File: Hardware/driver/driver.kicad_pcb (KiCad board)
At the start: 4 copper layers, 128.1 x 184.5 mm, 158 parts, among them J201 Conn_02x10_Odd_Even, J301 1017526, J401 TBP02R2W-381-03BE, J402 Conn_01x02_Male, J501 Conn_Coaxial, J601 Screw_Terminal_01x02, K601 EC2-5TNU, M201 Fan_4pin, Q201 MMBT3904, Q202 PN2222A, Q301 IXTH80N075L2, Q302 IXTH80N075L2, U101 ICL7660, U102 DS2482-100, U201 AT24CS32-SSHM, U202 NCP716BCSN330T1G, U203 ADUM1250, U204 FODM217B, U205 FODM217B, U206 EMC2101-R, U301 MCP3421A2T-ECH, U302 OPA2388, U303 DAC60501Z, U304 LM431SC, U305 MCP3421A3T-ECH, U306 OPA2388, U307 DAC60501Z, U308 LM431SC, U309 DS18B20, U310 DS18B20, U501 74LVC1G17, U502 FODM217B, U601 MCP3421A1T-ECH, U602 OPA277

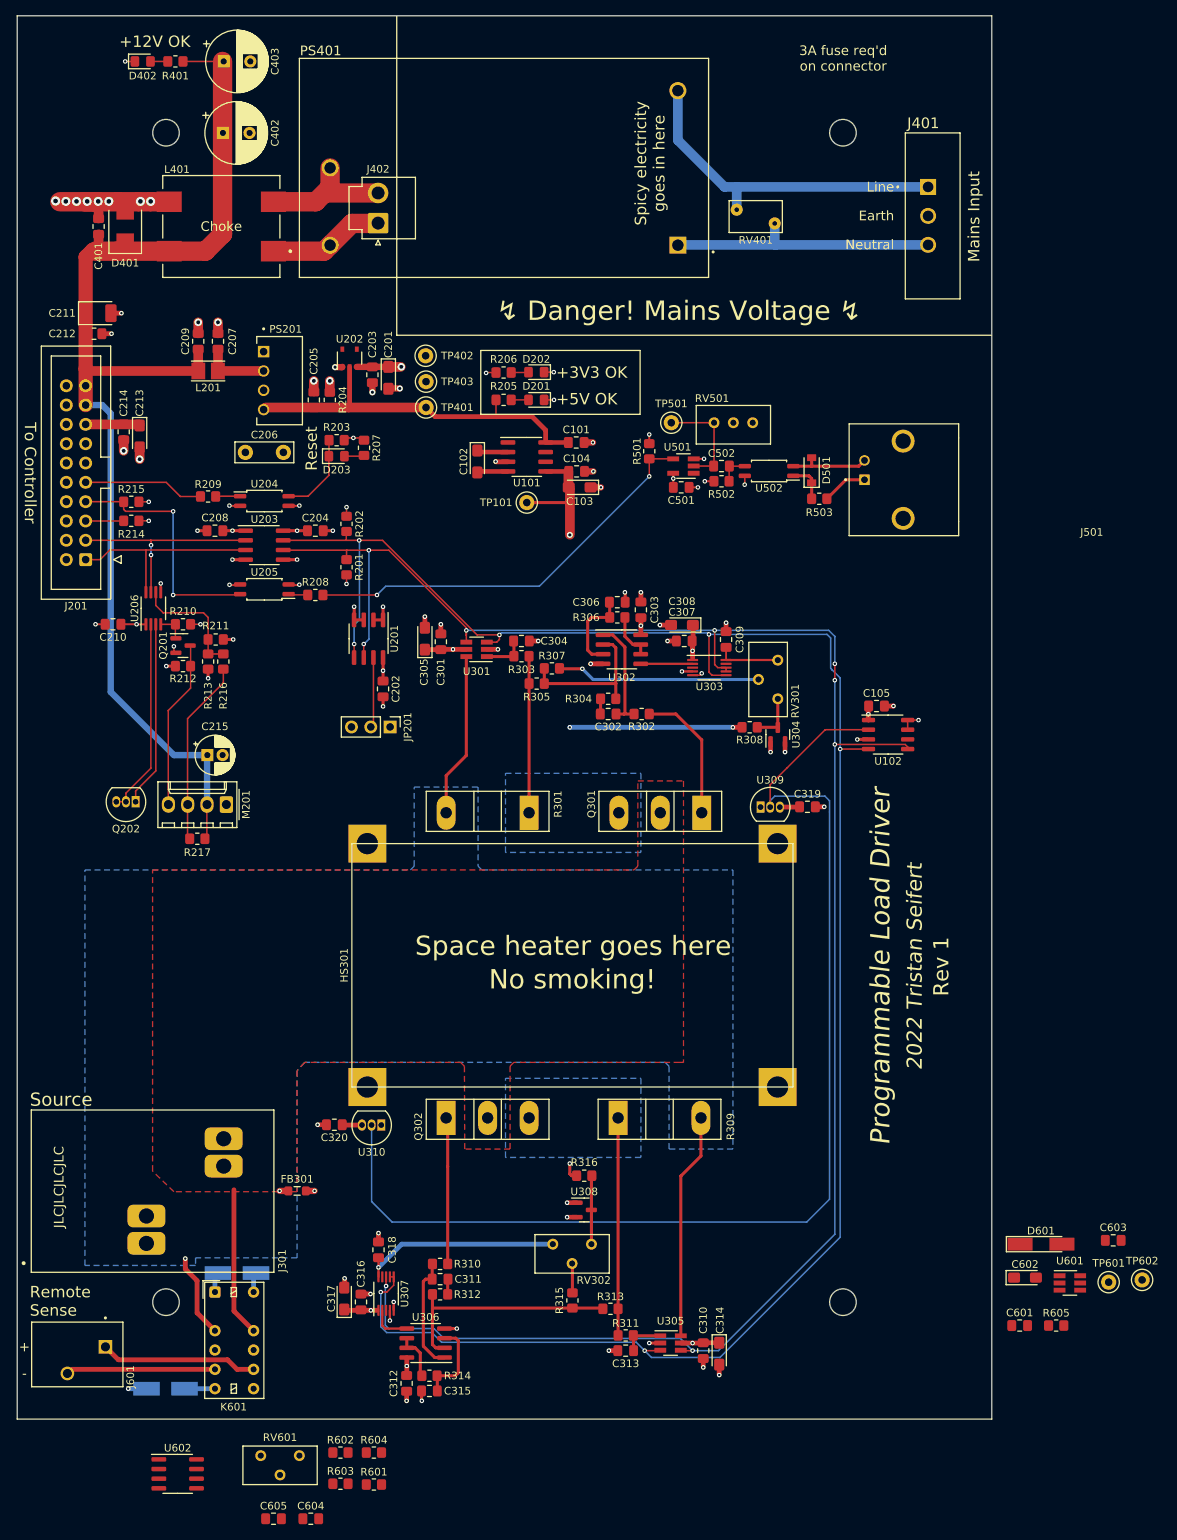
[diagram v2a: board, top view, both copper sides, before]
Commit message: Finished remote VSense support
- Laid out the VSense amp and analog-to-digital converter, as well as
  added an I2C IO expander to handle driving the latching relay to
  switch between internal and external sense.

  Also moved the input connector and some of the analog parts around to
  accomodate this all.

- Status indicator (with an extra GPIO on the IO expander) in the form
  of a single LED
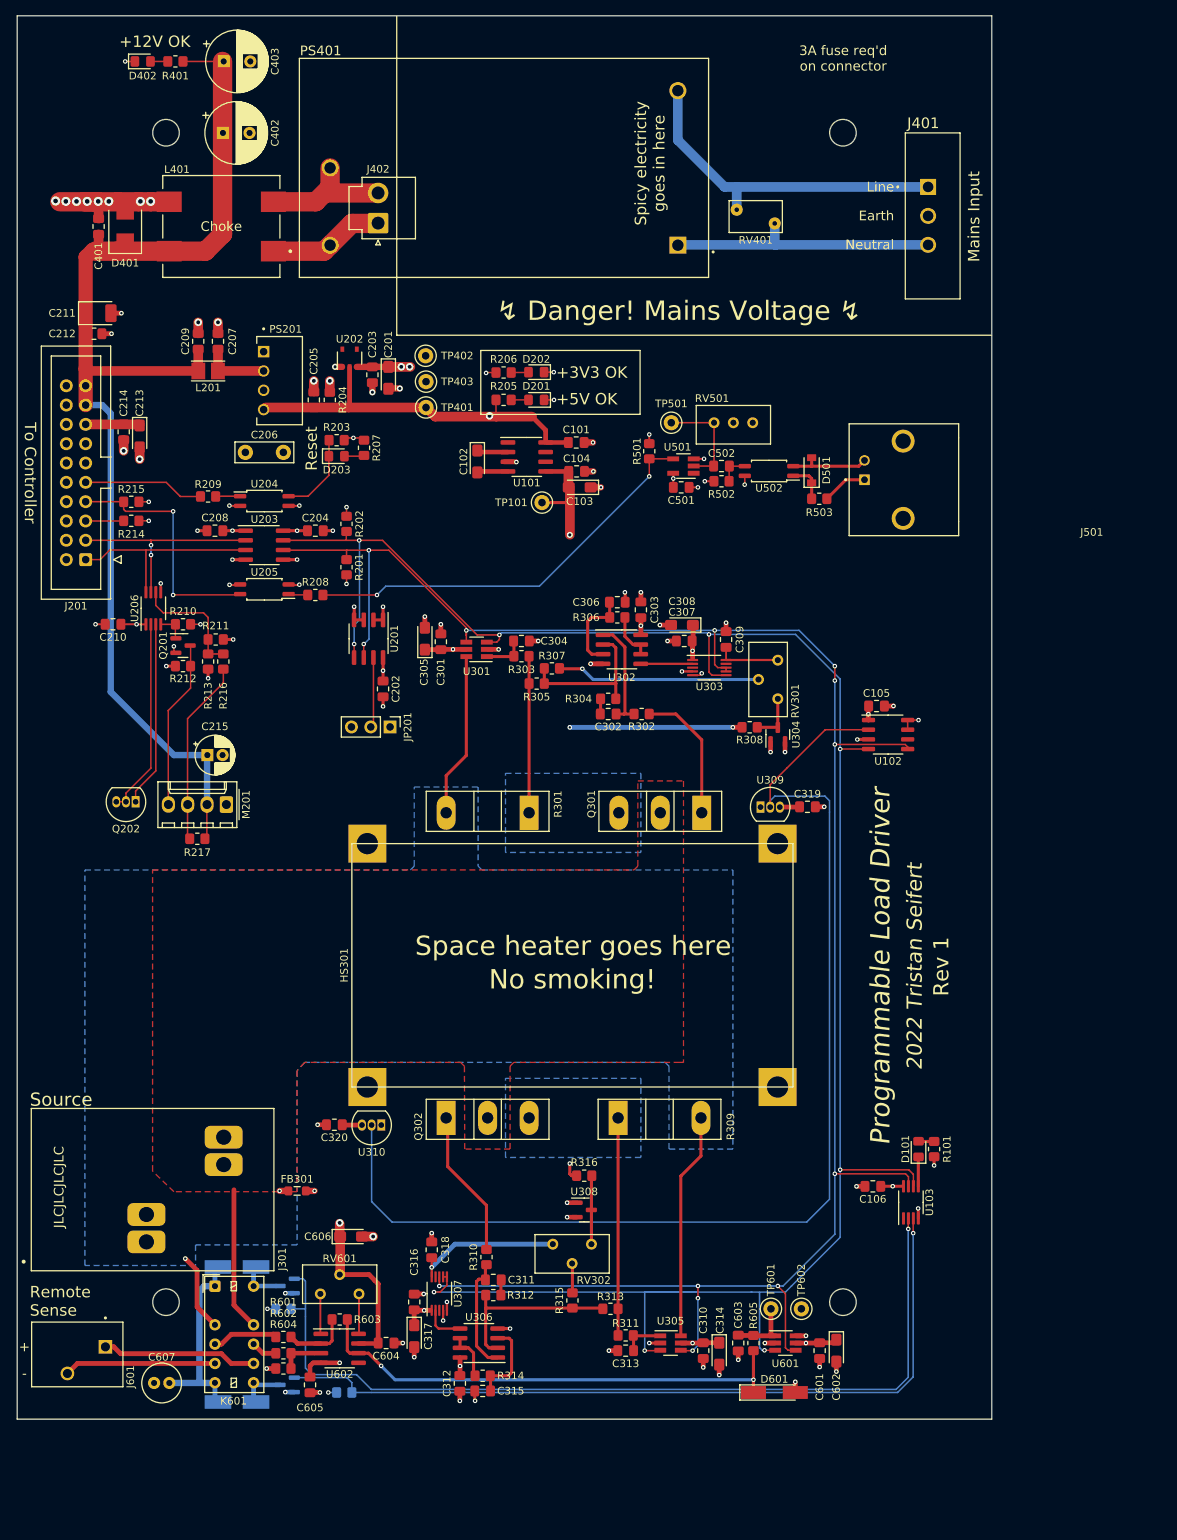
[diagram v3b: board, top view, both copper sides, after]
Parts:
- added C106: 100nF, Capacitor_SMD:C_0805_2012Metric_Pad1.18x1.45mm_HandSolder, F.Cu at (132.5, 173.9)
- added C606: 10µF, Capacitor_Tantalum_SMD:CP_EIA-3216-18_Kemet-A_Pad1.58x1.35mm_HandSolder, F.Cu at (63.9, 180.5)
- added C607: 10µF, Capacitor_THT:C_Radial_D5.0mm_H11.0mm_P2.00mm, F.Cu at (40.0, 199.8)
- added D101: Red, LED_SMD:LED_0805_2012Metric_Pad1.15x1.40mm_HandSolder, F.Cu at (138.5, 169.0)
- added Q601: MMBT3904, Package_TO_SOT_SMD:SOT-23, B.Cu at (55.5, 200.0)
- added Q602: MMBT3904, Package_TO_SOT_SMD:SOT-23, B.Cu at (55.5, 187.0)
- added R101: 1k, Resistor_SMD:R_0805_2012Metric_Pad1.20x1.40mm_HandSolder, F.Cu at (140.6, 169.0)
- added R606: 10k, Resistor_SMD:R_0805_2012Metric_Pad1.20x1.40mm_HandSolder, B.Cu at (55.0, 190.0)
- added R607: 10k, Resistor_SMD:R_0805_2012Metric_Pad1.20x1.40mm_HandSolder, B.Cu at (63.0, 201.0)
- added U103: PI4IOE5V9536, Package_SO:MSOP-8_3x3mm_P0.65mm, F.Cu at (137.5, 176.0)
- moved C603 51.1 mm to (114.8, 194.5), turned to -90 degrees
- moved TP602 45.0 mm to (123.1, 190.0)
- moved TP601 44.5 mm to (119.1, 190.0)
- moved D601 40.1 mm to (119.5, 201.0)
- moved R605 39.9 mm to (116.8, 194.5), turned to -90 degrees
- moved U601 38.2 mm to (121.0, 194.5)
- moved U602 26.9 mm to (62.4, 195.2)
- moved C602 26.6 mm to (127.7, 195.5), turned to -90 degrees
- moved C601 26.5 mm to (125.5, 195.5), turned to -90 degrees
- moved C604 25.1 mm to (68.5, 194.5)
- moved R601 22.8 mm to (55.0, 193.7), turned to 180 degrees
- moved R603 21.6 mm to (62.4, 191.4), turned to 180 degrees
- moved RV601 21.4 mm to (59.9, 188.0), turned to 180 degrees
- moved C605 18.2 mm to (58.5, 200.0), turned to -90 degrees
- moved R604 16.2 mm to (55.0, 197.8), turned to 180 degrees
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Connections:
- D602 pad 1: /Input Stage/Voltage Sense/SEL_SET -> +5V
- D602 pad 2: GND -> /Input Stage/Voltage Sense/SEL_SET
- D603 pad 1: /Input Stage/Voltage Sense/SEL_RESET -> +5V
- D603 pad 2: GND -> /Input Stage/Voltage Sense/SEL_RESET
- K601 pad 1: /Input Stage/Voltage Sense/SEL_SET -> +5V
- K601 pad 12: GND -> /Input Stage/Voltage Sense/SEL_SET
- K601 pad 6: /Input Stage/Voltage Sense/SEL_RESET -> +5V
- K601 pad 7: GND -> /Input Stage/Voltage Sense/SEL_RESET
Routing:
- net +5V: track 50.3 -> 233.5 mm, vias 0 -> 2
- net /SENSE_SET: track 0.00 -> 116.9 mm, vias 0 -> 1
- net /SENSE_RST: track 0.00 -> 104.6 mm, vias 0 -> 1
- net /Input Stage/Voltage Sense/VSENSE: track 0.00 -> 64.6 mm, vias 0 -> 2
- net -5V: track 124.5 -> 174.7 mm, vias 4 -> 5
- net /I2C_SCL: track 266.3 -> 282.5 mm, vias 7 -> 9
- net GND: track 83.6 -> 98.4 mm, vias 55 -> 70
- net +3V3: track 55.2 -> 66.1 mm, vias 18 -> 22
- net /I2C_SDA: track 265.4 -> 275.8 mm, vias 9 -> 13
- net Net-(R601-Pad1): track 0.00 -> 8.71 mm
- net /Input Stage/Voltage Sense/VIN-: track 0.00 -> 8.68 mm
- net Net-(C603-Pad1): track 0.00 -> 8.46 mm
- net Net-(R312-Pad2): track 30.8 -> 23.8 mm
- net /Input Stage/VREF1: track 26.1 -> 19.1 mm
- net Net-(RV601-Pad3): track 0.00 -> 5.28 mm
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
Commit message: Layout tweaks to driver
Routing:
- net /Mains Supply (Optional)/MAINS_L: track 45.0 -> 45.7 mm
- net /Mains Supply (Optional)/MAINS_N: track 35.8 -> 36.5 mm
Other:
- board text added: "(jk, just a bunch of copper)"
- board text added: "Box filled with magic smoke"
- board text added: "Olympic-size swimming pool"
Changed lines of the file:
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@@
     (property "Sheetname" "Input Stage")
     (attr smd)
-    (fp_text reference "R302" (at 0 -1.65) (layer "F.SilkS")
+    (fp_text reference "R302" (at 0 1.65) (layer "F.SilkS")
       (effects (font (size 1 1) (thickness 0.15)))
     )
@@
   (gr_line (start 148.1 62) (end 69.9 62) (layer "F.SilkS") (width 0.15))
   (gr_line (start 80.95 72.4) (end 101.85 72.4) (layer "F.SilkS") (width 0.15))
+  (gr_line (start 104.5 120.5) (end 104.9 120.15) (layer "F.SilkS") (width 0.15))
+  (gr_line (start 104.5 120.5) (end 104.1 120.15) (layer "F.SilkS") (width 0.15))
   (gr_line (start 101.9 72.4) (end 101.9 64) (layer "F.SilkS") (width 0.15))
   (gr_line (start 69.9 62) (end 69.9 20) (layer "F.SilkS") (width 0.15))
   (gr_line (start 101.85 64) (end 80.95 64) (layer "F.SilkS") (width 0.15))
   (gr_line (start 80.95 64) (end 80.95 72.4) (layer "F.SilkS") (width 0.15))
+  (gr_line (start 104.5 119) (end 104.5 120.5) (layer "F.SilkS") (width 0.15))
   (gr_line (start 20 204.5) (end 148.13 204.5) (layer "Edge.Cuts") (width 0.1))
   (gr_line (start 148.13 20) (end 148.13 204.5) (layer "Edge.Cuts") (width 0.1))
   (gr_line (start 20 20) (end 148.13 20) (layer "Edge.Cuts") (width 0.1))
   (gr_line (start 20 20) (end 20 204.5) (layer "Edge.Cuts") (width 0.1))
+  (gr_text "Olympic-size swimming pool" (at 67.5 138) (layer "B.SilkS")
+    (effects (font (size 2 2) (thickness 0.25)) (justify mirror))
+  )
+  (gr_text "(jk, just a bunch of copper)" (at 67.5 141.5) (layer "B.SilkS")
+    (effects (font (size 1.5 1.5) (thickness 0.2) italic) (justify mirror))
+  )
   (gr_text "No touching – it will hurt!\n(Unless you're into that stuff)" (at 120 41.2) (layer "B.SilkS")
     (effects (font (size 1.5 1.5) (thickness 0.15)) (justify mirror))
@@
     (effects (font (size 1.5 1.5) (thickness 0.25)) (justify left))
   )
-  (gr_text "Source" (at 21.65 162.5) (layer "F.SilkS")
+  (gr_text "Source" (at 21.65 162.2) (layer "F.SilkS")
     (effects (font (size 1.74 1.74) (thickness 0.25)) (justify left))
   )
@@
     (effects (font (size 1.5 1.5) (thickness 0.25)) (justify left))
   )
+  (gr_text "Box filled with\nmagic smoke" (at 104.6 117) (layer "F.SilkS")
+    (effects (font (size 1.5 1.5) (thickness 0.2)))
+  )
   (segment (start 64.2 75.5) (end 65.3 75.5) (width 0.2032) (layer "F.Cu") (net 1))
   (segment (start 76.5 190.2) (end 76.5 189.1) (width 0.3) (layer "F.Cu") (net 1))
@@
   (segment (start 108.8 105.2) (end 101.98 105.2) (width 0.3) (layer "F.Cu") (net 29))
   (segment (start 101.98 105.2) (end 101.975 105.205) (width 0.254) (layer "F.Cu") (net 29))
-  (segment (start 119.72 50.12) (end 106.9 50.12) (width 1.27) (layer "B.Cu") (net 30))
+  (segment (start 119.72 50.12) (end 106.2 50.12) (width 2.54) (layer "B.Cu") (net 30))
   (segment (start 106.9 50.12) (end 106.86 50.16) (width 1.27) (layer "B.Cu") (net 30))
-  (segment (start 139.7625 50.12) (end 119.72 50.12) (width 1.27) (layer "B.Cu") (net 30))
+  (segment (start 139.7625 50.12) (end 119.72 50.12) (width 2.54) (layer "B.Cu") (net 30))
   (segment (start 119.6 50) (end 119.72 50.12) (width 1.27) (layer "B.Cu") (net 30))
-  (segment (start 119.6 47.3) (end 119.6 50) (width 1.27) (layer "B.Cu") (net 30))
-  (segment (start 114.6 45.5) (end 114.6 42.5) (width 1.27) (layer "B.Cu") (net 32))
-  (segment (start 106.86 36.36) (end 106.86 29.84) (width 1.27) (layer "B.Cu") (net 32))
-  (segment (start 139.7625 42.5) (end 114.6 42.5) (width 1.27) (layer "B.Cu") (net 32))
-  (segment (start 114.6 42.5) (end 113 42.5) (width 1.27) (layer "B.Cu") (net 32))
-  (segment (start 113 42.5) (end 106.86 36.36) (width 1.27) (layer "B.Cu") (net 32))
+  (segment (start 119.6 47.3) (end 119.6 50) (width 2.54) (layer "B.Cu") (net 30))
+  (segment (start 114.6 45.5) (end 114.6 42.5) (width 2.54) (layer "B.Cu") (net 32))
+  (segment (start 106.86 36.36) (end 106.86 29.84) (width 2.54) (layer "B.Cu") (net 32))
+  (segment (start 140.5 42.5) (end 114.6 42.5) (width 2.54) (layer "B.Cu") (net 32))
+  (segment (start 114.6 42.5) (end 113 42.5) (width 2.54) (layer "B.Cu") (net 32))
+  (segment (start 113 42.5) (end 106.86 36.36) (width 2.54) (layer "B.Cu") (net 32))
   (segment (start 83.175 193.865) (end 84.665 193.865) (width 0.4064) (layer "F.Cu") (net 33))
   (segment (start 82.2375 198.8375) (end 82.2 198.8) (width 0.4064) (layer "F.Cu") (net 33))
